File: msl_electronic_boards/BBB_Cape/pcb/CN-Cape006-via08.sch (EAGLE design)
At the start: 99 parts, among them IC3 LM340MP-05, IC4 LM2576, IC5 LM2575, P8 BeagleBoard 2x23, P9 BeagleBoard 2x23, U1 ADUM1200ARZ, U2 ADUM1300ARWZ, U3 ADUM1200ARZ, U4 ADUM1300ARWZ

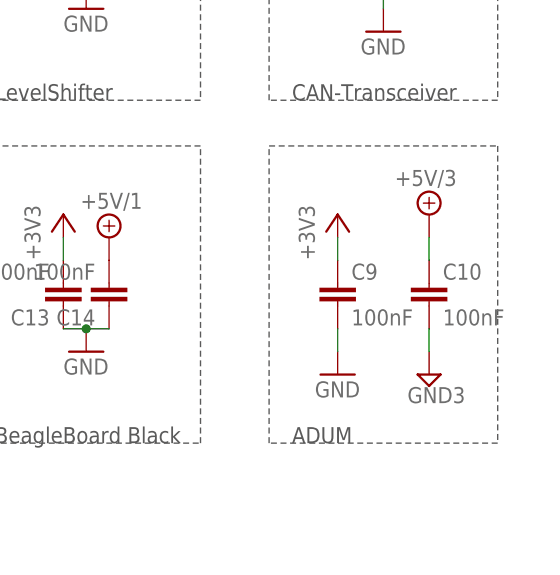
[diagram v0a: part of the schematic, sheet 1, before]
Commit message: BBB - Task 155 - apply changed conductor tracks
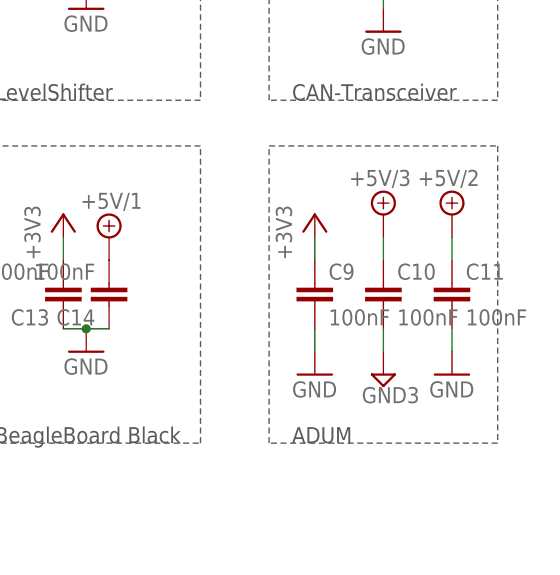
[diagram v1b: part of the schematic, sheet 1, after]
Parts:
- added C11: 100nF, rcl:C-EUC0603
- CAN: value (none) -> RJ10; device con-weidmueller-sl35:90-4 -> ownParts:RJ10
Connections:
- removed net 5V/2_F&J: CAN.4, SJ1.1
- new net N$19: CAN.P$1, SJ1.1
- net +3V3: no longer U2.VDD1, U4.VDD1
- net +5V/2: now also C11.1, U2.VDD1, U4.VDD1
- net CANH: now also CAN.P$3; no longer CAN.2
- net CANL: now also CAN.P$2; no longer CAN.3
- net GND: now also C11.2, CAN.P$4; no longer CAN.1
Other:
- moved on the sheet: C10, C9, CAN
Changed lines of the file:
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@@
 <?xml version="1.0" encoding="utf-8"?>
 <!DOCTYPE eagle SYSTEM "eagle.dtd">
-<eagle version="7.2.0">
+<eagle version="7.5.0">
 <drawing>
 <settings>
@@
 <part name="R1" library="rcl" deviceset="R-EU_" device="R0805" value="1k"/>
 <part name="R2" library="rcl" deviceset="R-EU_" device="R0805" value="120"/>
-<part name="CAN" library="con-weidmueller-sl35" deviceset="90-4" device=""/>
 <part name="SJ1" library="jumper" deviceset="SJ" device=""/>
 <part name="SJ2" library="jumper" deviceset="SJ" device=""/>
@@
 <part name="GND19" library="supply1" deviceset="GND" device=""/>
 <part name="GND3" library="supply1" deviceset="GND" device=""/>
-<part name="+3V4" library="supply1" deviceset="+3V3" device=""/>
 <part name="+3V8" library="supply1" deviceset="+3V3" device=""/>
 <part name="GND21" library="supply1" deviceset="GND" device=""/>
@@
 <part name="U2" library="ADUM1300" deviceset="ADUM1300ARWZ" device=""/>
 <part name="GND22" library="supply1" deviceset="GND" device=""/>
-<part name="+3V9" library="supply1" deviceset="+3V3" device=""/>
 <part name="+3V10" library="supply1" deviceset="+3V3" device=""/>
 <part name="GND23" library="supply1" deviceset="GND" device=""/>
@@
 <part name="GND7" library="supply1" deviceset="GND" device=""/>
 <part name="FRAME2" library="frames" deviceset="A4P-LOC" device=""/>
+<part name="SUPPLY17" library="supply2" deviceset="+5V/2" device=""/>
+<part name="SUPPLY30" library="supply2" deviceset="+5V/2" device=""/>
+<part name="SUPPLY31" library="supply2" deviceset="+5V/2" device=""/>
+<part name="GND29" library="supply1" deviceset="GND" device=""/>
+<part name="C11" library="rcl" deviceset="C-EU" device="C0603" value="100nF"/>
+<part name="CAN" library="ownParts" deviceset="RJ10" device=""/>
 </parts>
 <sheets>
@@
 <instance part="5V3" gate="G$1" x="58.42" y="132.08"/>
 <instance part="R8" gate="G$1" x="58.42" y="142.24" rot="R90"/>
-<instance part="C9" gate="G$1" x="152.4" y="200.66"/>
-<instance part="C10" gate="G$1" x="162.56" y="200.66"/>
-<instance part="+3V7" gate="G$1" x="152.4" y="208.28"/>
-<instance part="GND17" gate="1" x="152.4" y="190.5"/>
-<instance part="SUPPLY2" gate="G$1" x="162.56" y="208.28"/>
-<instance part="SUPPLY22" gate="G$1" x="162.56" y="190.5"/>
+<instance part="C9" gate="G$1" x="149.86" y="200.66"/>
+<instance part="C10" gate="G$1" x="157.48" y="200.66"/>
+<instance part="+3V7" gate="G$1" x="149.86" y="208.28"/>
+<instance part="GND17" gate="1" x="149.86" y="190.5"/>
+<instance part="SUPPLY2" gate="G$1" x="157.48" y="208.28"/>
+<instance part="SUPPLY22" gate="G$1" x="157.48" y="190.5"/>
 <instance part="FRAME2" gate="G$1" x="0" y="0"/>
+<instance part="SUPPLY31" gate="G$1" x="165.1" y="208.28"/>
+<instance part="GND29" gate="1" x="165.1" y="190.5"/>
+<instance part="C11" gate="G$1" x="165.1" y="200.66"/>
 </instances>
 <busses>
@@
 <pinref part="GND17" gate="1" pin="GND"/>
 <pinref part="C9" gate="G$1" pin="2"/>
-<wire x1="152.4" y1="193.04" x2="152.4" y2="195.58" width="0.1524" layer="91"/>
+<wire x1="149.86" y1="193.04" x2="149.86" y2="195.58" width="0.1524" layer="91"/>
+</segment>
+<segment>
+<pinref part="C11" gate="G$1" pin="2"/>
+<pinref part="GND29" gate="1" pin="GND"/>
+<wire x1="165.1" y1="195.58" x2="165.1" y2="193.04" width="0.1524" layer="91"/>
 </segment>
 </net>
@@
 <junction x="76.2" y="187.96"/>
 </segment>
+<segment>
+<pinref part="SUPPLY31" gate="G$1" pin="+5V/2"/>
+<pinref part="C11" gate="G$1" pin="1"/>
+<wire x1="165.1" y1="205.74" x2="165.1" y2="203.2" width="0.1524" layer="91"/>
+</segment>
 </net>
 <net name="+24V" class="0">
@@
 <pinref part="C9" gate="G$1" pin="1"/>
 <pinref part="+3V7" gate="G$1" pin="+3V3"/>
-<wire x1="152.4" y1="203.2" x2="152.4" y2="205.74" width="0.1524" layer="91"/>
+<wire x1="149.86" y1="203.2" x2="149.86" y2="205.74" width="0.1524" layer="91"/>
 </segment>
 </net>
@@
 <pinref part="SUPPLY2" gate="G$1" pin="+5V/3"/>
 <pinref part="C10" gate="G$1" pin="1"/>
-<wire x1="162.56" y1="205.74" x2="162.56" y2="203.2" width="0.1524" layer="91"/>
+<wire x1="157.48" y1="205.74" x2="157.48" y2="203.2" width="0.1524" layer="91"/>
 </segment>
 </net>
@@
 <pinref part="C10" gate="G$1" pin="2"/>
 <pinref part="SUPPLY22" gate="G$1" pin="GND3"/>
-<wire x1="162.56" y1="195.58" x2="162.56" y2="193.04" width="0.1524" layer="91"/>
+<wire x1="157.48" y1="195.58" x2="157.48" y2="193.04" width="0.1524" layer="91"/>
 </segment>
 </net>
@@
 <instance part="GND2" gate="1" x="137.16" y="45.72"/>
 <instance part="SUPPLY4" gate="G$1" x="215.9" y="124.46"/>
-<instance part="CAN" gate="G$1" x="149.86" y="119.38"/>
 <instance part="SJ1" gate="1" x="142.24" y="114.3" rot="R180"/>
 <instance part="CON_STECKERBOX" gate="G$1" x="160.02" y="154.94" rot="R180"/>
@@
 <instance part="JP4" gate="G$1" x="88.9" y="17.78"/>
 <instance part="GND5" gate="1" x="68.58" y="15.24"/>
+<instance part="CAN" gate="G$1" x="152.4" y="119.38"/>
 </instances>
 <busses>
@@
 <segment>
 <pinref part="GND16" gate="1" pin="GND"/>
-<pinref part="CAN" gate="G$1" pin="1"/>
-<wire x1="147.32" y1="121.92" x2="134.62" y2="121.92" width="0.1524" layer="91"/>
+<wire x1="149.86" y1="121.92" x2="134.62" y2="121.92" width="0.1524" layer="91"/>
 <wire x1="134.62" y1="121.92" x2="134.62" y2="111.76" width="0.1524" layer="91"/>
+<pinref part="CAN" gate="G$1" pin="P$4"/>
 </segment>
 <segment>
@@
 <net name="CANL" class="0">
 <segment>
-<wire x1="147.32" y1="116.84" x2="129.54" y2="116.84" width="0.1524" layer="91"/>
+<wire x1="149.86" y1="116.84" x2="129.54" y2="116.84" width="0.1524" layer="91"/>
 <label x="129.54" y="116.84" size="1.778" layer="95" rot="R180" xref="yes"/>
-<pinref part="CAN" gate="G$1" pin="3"/>
+<pinref part="CAN" gate="G$1" pin="P$2"/>
 </segment>
 </net>
 <net name="CANH" class="0">
 <segment>
-<wire x1="147.32" y1="119.38" x2="129.54" y2="119.38" width="0.1524" layer="91"/>
+<wire x1="149.86" y1="119.38" x2="129.54" y2="119.38" width="0.1524" layer="91"/>
 <label x="129.54" y="119.38" size="1.778" layer="95" rot="R180" xref="yes"/>
-<pinref part="CAN" gate="G$1" pin="2"/>
-</segment>
-</net>
-<net name="5V/2_F&amp;J" class="0">
-<segment>
-<pinref part="SJ1" gate="1" pin="1"/>
-<pinref part="CAN" gate="G$1" pin="4"/>
+<pinref part="CAN" gate="G$1" pin="P$3"/>
 </segment>
 </net>
@@
 <wire x1="27.94" y1="20.32" x2="25.4" y2="20.32" width="0.1524" layer="91"/>
 <wire x1="25.4" y1="20.32" x2="25.4" y2="22.86" width="0.1524" layer="91"/>
+</segment>
+</net>
+<net name="N$19" class="0">
+<segment>
+<pinref part="SJ1" gate="1" pin="1"/>
+<pinref part="CAN" gate="G$1" pin="P$1"/>
+<wire x1="149.86" y1="114.3" x2="147.32" y2="114.3" width="0.1524" layer="91"/>
 </segment>
 </net>
@@
 <instance part="U4" gate="A" x="99.06" y="66.04"/>
 <instance part="GND3" gate="1" x="76.2" y="35.56"/>
-<instance part="+3V4" gate="G$1" x="76.2" y="91.44"/>
 <instance part="+3V8" gate="G$1" x="124.46" y="96.52" rot="R180"/>
 <instance part="GND21" gate="1" x="119.38" y="124.46" rot="R180"/>
@@
 <instance part="U2" gate="A" x="99.06" y="177.8"/>
 <instance part="GND22" gate="1" x="76.2" y="147.32"/>
-<instance part="+3V9" gate="G$1" x="76.2" y="203.2"/>
 <instance part="+3V10" gate="G$1" x="124.46" y="208.28" rot="R180"/>
 <instance part="GND23" gate="1" x="119.38" y="236.22" rot="R180"/>
@@
 <attribute name="REICHELT" x="152.4" y="68.58" size="1.778" layer="96" rot="R180" display="off"/>
 </instance>
+<instance part="SUPPLY17" gate="G$1" x="76.2" y="203.2"/>
+<instance part="SUPPLY30" gate="G$1" x="76.2" y="91.44"/>
 </instances>
 <busses>
@@
 <net name="+3V3" class="0">
 <segment>
-<pinref part="U4" gate="A" pin="VDD1"/>
-<pinref part="+3V4" gate="G$1" pin="+3V3"/>
-<wire x1="81.28" y1="83.82" x2="76.2" y2="83.82" width="0.1524" layer="91"/>
-<wire x1="76.2" y1="83.82" x2="76.2" y2="88.9" width="0.1524" layer="91"/>
-</segment>
-<segment>
 <pinref part="U3" gate="A" pin="VDD2"/>
 <pinref part="+3V8" gate="G$1" pin="+3V3"/>
 <wire x1="116.84" y1="104.14" x2="124.46" y2="104.14" width="0.1524" layer="91"/>
 <wire x1="124.46" y1="104.14" x2="124.46" y2="99.06" width="0.1524" layer="91"/>
-</segment>
-<segment>
-<pinref part="U2" gate="A" pin="VDD1"/>
-<pinref part="+3V9" gate="G$1" pin="+3V3"/>
-<wire x1="81.28" y1="195.58" x2="76.2" y2="195.58" width="0.1524" layer="91"/>
-<wire x1="76.2" y1="195.58" x2="76.2" y2="200.66" width="0.1524" layer="91"/>
 </segment>
 <segment>
@@
 </segment>
 </net>
+<net name="+5V/2" class="0">
+<segment>
+<pinref part="U2" gate="A" pin="VDD1"/>
+<pinref part="SUPPLY17" gate="G$1" pin="+5V/2"/>
+<wire x1="81.28" y1="195.58" x2="76.2" y2="195.58" width="0.1524" layer="91"/>
+<wire x1="76.2" y1="195.58" x2="76.2" y2="200.66" width="0.1524" layer="91"/>
+</segment>
+<segment>
+<pinref part="U4" gate="A" pin="VDD1"/>
+<pinref part="SUPPLY30" gate="G$1" pin="+5V/2"/>
+<wire x1="81.28" y1="83.82" x2="76.2" y2="83.82" width="0.1524" layer="91"/>
+<wire x1="76.2" y1="83.82" x2="76.2" y2="88.9" width="0.1524" layer="91"/>
+</segment>
+</net>
